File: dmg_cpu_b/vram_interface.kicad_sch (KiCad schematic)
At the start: 177 parts

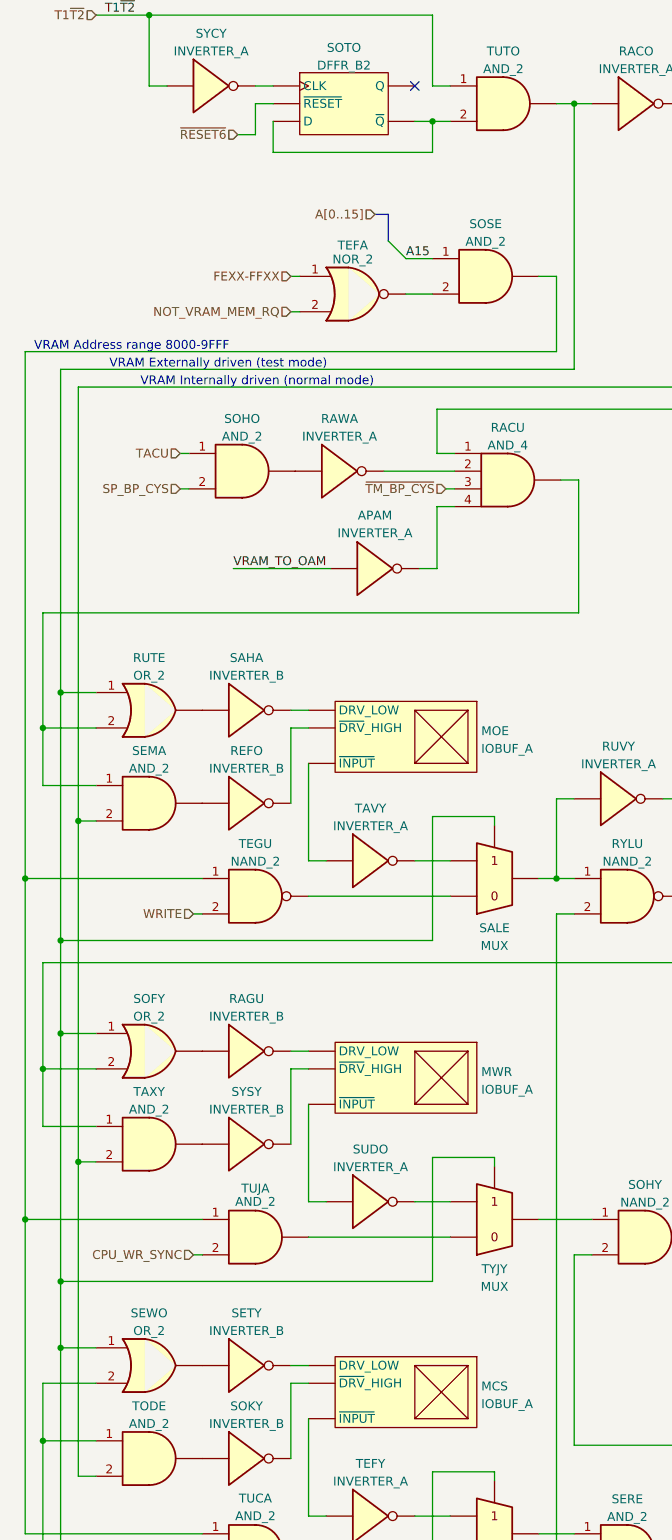
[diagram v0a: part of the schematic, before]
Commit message: Issues addressed. Renaming and inverted signal names to make thing more consistent and meaningful.
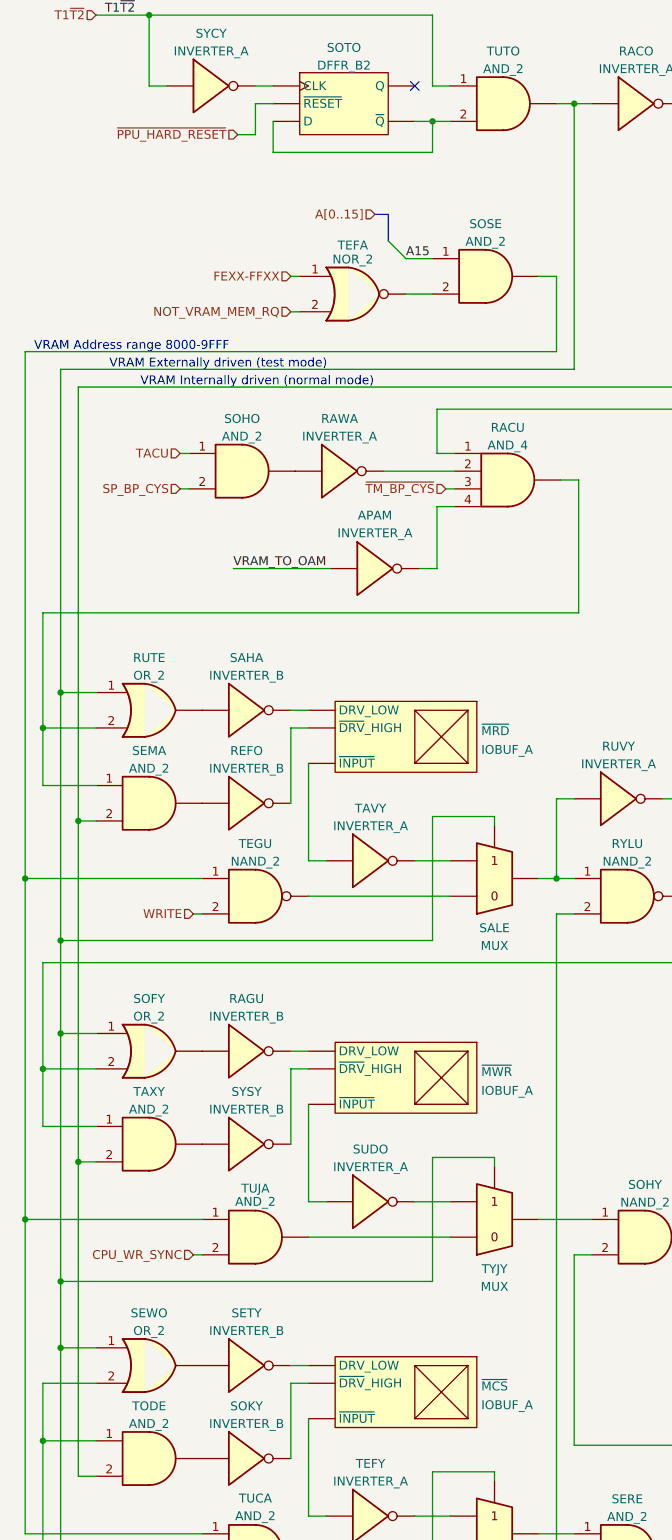
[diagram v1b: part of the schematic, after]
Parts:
- renumbered MCS to ~{MCS}, MOE to ~{MRD}, MWR to ~{MWR}
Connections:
- net ~{RESET6} renamed ~{PPU_HARD_RESET}
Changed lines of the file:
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@@
     (effects (font (size 1.27 1.27)) (justify right))
   )
-  (hierarchical_label "~{RESET6}" (shape input) (at 47.625 55.245 180)
+  (hierarchical_label "~{PPU_HARD_RESET}" (shape input) (at 47.625 55.245 180)
     (effects (font (size 1.27 1.27)) (justify right))
   )
@@
   (symbol (lib_id "DMG_CPU_Cells:IOBUF_A") (at 71.755 141.605 0) (mirror y) (unit 1)
     (in_bom yes) (on_board yes) (fields_autoplaced)
-    (property "Reference" "MOE" (id 0) (at 82.55 140.7703 0)
-      (effects (font (size 1.27 1.27)) (justify right))
-    )
-    (property "Value" "IOBUF_A" (id 1) (at 82.55 143.3072 0)
+    (property "Reference" "~{MRD}" (id 0) (at 82.55 140.7703 0)
+      (effects (font (size 1.27 1.27)) (justify right))
+    )
+    (property "Value" "IOBUF_A" (id 1) (at 82.55 143.4612 0)
       (effects (font (size 1.27 1.27)) (justify right))
     )
@@
   (symbol (lib_id "DMG_CPU_Cells:IOBUF_A") (at 71.755 235.585 0) (mirror y) (unit 1)
     (in_bom yes) (on_board yes) (fields_autoplaced)
-    (property "Reference" "MCS" (id 0) (at 82.55 234.7503 0)
-      (effects (font (size 1.27 1.27)) (justify right))
-    )
-    (property "Value" "IOBUF_A" (id 1) (at 82.55 237.2872 0)
+    (property "Reference" "~{MCS}" (id 0) (at 82.55 234.7503 0)
+      (effects (font (size 1.27 1.27)) (justify right))
+    )
+    (property "Value" "IOBUF_A" (id 1) (at 82.55 237.4412 0)
       (effects (font (size 1.27 1.27)) (justify right))
     )
@@
   (symbol (lib_id "DMG_CPU_Cells:IOBUF_A") (at 71.755 190.5 0) (mirror y) (unit 1)
     (in_bom yes) (on_board yes) (fields_autoplaced)
-    (property "Reference" "MWR" (id 0) (at 82.55 189.6653 0)
-      (effects (font (size 1.27 1.27)) (justify right))
-    )
-    (property "Value" "IOBUF_A" (id 1) (at 82.55 192.2022 0)
-      (effects (font (size 1.27 1.27)) (justify right))
-    )
+    (property "Reference" "~{MWR}" (id 0) (at 82.55 189.6653 0)
+      (effects (font (size 1.27 1.27)) (justify right))
+    )
+    (property "Value" "IOBUF_A" (id 1) (at 82.55 192.3562 0)
+      (effects (font (size 1.27 1.27)) (justify right))
+    )

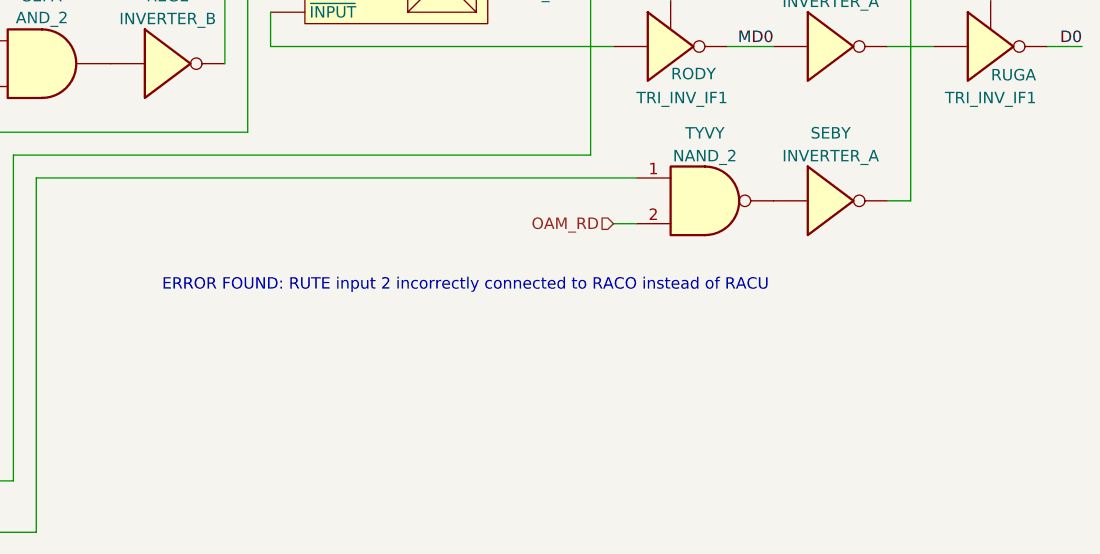
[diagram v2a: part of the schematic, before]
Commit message: Unnecessary comments removed. Data buffers moved to CPU page.
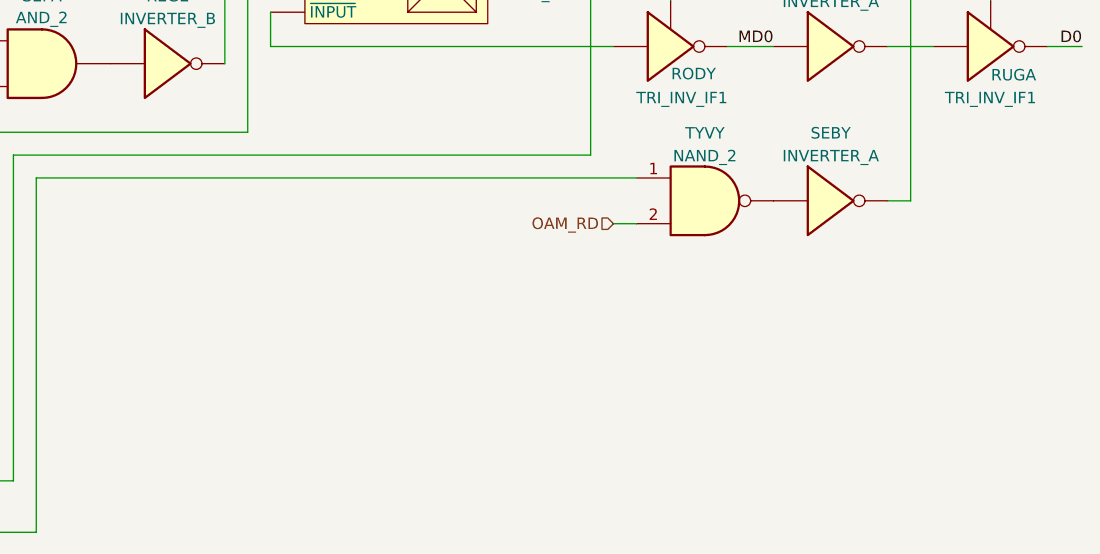
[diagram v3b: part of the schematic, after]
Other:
- note removed: "ERROR FOUND: RUTE input 2 incorrectly connected to RACO instead of RACU"
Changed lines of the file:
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@@
-    (effects (font (size 1.27 1.27)) (justify left bottom))
-  )
-  (text "ERROR FOUND: RUTE input 2 incorrectly connected to RACO instead of RACU"
-    (at 303.53 256.54 0)
     (effects (font (size 1.27 1.27)) (justify left bottom))
   )

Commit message: Update - edits were done some time ago so cannot rcall what has been done.
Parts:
- renumbered SAHA to RONU, SETY to ROSU
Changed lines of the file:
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@@
   (symbol (lib_id "DMG_CPU_Cells:INVERTER_B") (at 48.895 137.795 0) (unit 1)
     (in_bom yes) (on_board yes) (fields_autoplaced)
-    (property "Reference" "SAHA" (id 0) (at 48.895 130.2852 0))
+    (property "Reference" "RONU" (id 0) (at 48.895 130.2852 0))
     (property "Value" "INVERTER_B" (id 1) (at 48.895 132.8221 0))
     (property "Footprint" "" (id 2) (at 46.355 137.795 0)
@@
   (symbol (lib_id "DMG_CPU_Cells:INVERTER_B") (at 48.895 231.775 0) (unit 1)
     (in_bom yes) (on_board yes) (fields_autoplaced)
-    (property "Reference" "SETY" (id 0) (at 48.895 224.2652 0))
+    (property "Reference" "ROSU" (id 0) (at 48.895 224.2652 0))
     (property "Value" "INVERTER_B" (id 1) (at 48.895 226.8021 0))
     (property "Footprint" "" (id 2) (at 46.355 231.775 0)

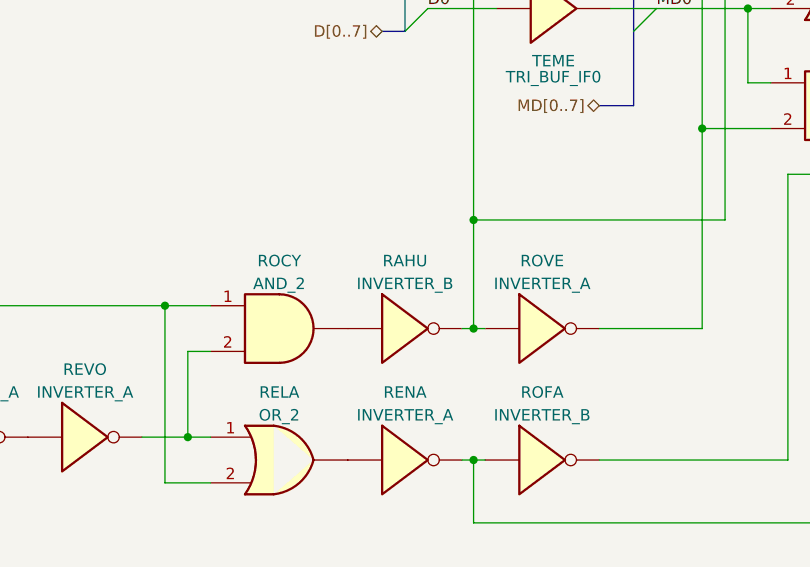
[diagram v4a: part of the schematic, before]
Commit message: Fix done based on github tickets #152 to #155
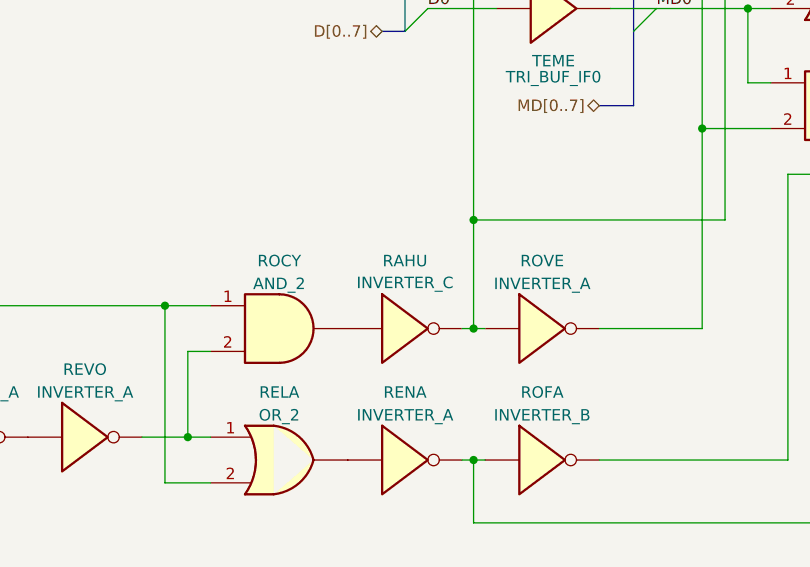
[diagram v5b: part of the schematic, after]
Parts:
- RAHU: value INVERTER_B -> INVERTER_C; symbol DMG_CPU_Cells:INVERTER_B -> DMG_CPU_Cells:INVERTER_C
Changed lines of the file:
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@@
     (pin "4")
   )
-  (symbol (lib_id "DMG_CPU_Cells:INVERTER_B") (at 241.935 255.905 0) (unit 1)
-    (in_bom yes) (on_board yes) (fields_autoplaced)
+  (symbol (lib_id "DMG_CPU_Cells:INVERTER_C") (at 241.935 255.905 0) (unit 1)
+    (in_bom yes) (on_board yes)
     (property "Reference" "RAHU" (id 0) (at 241.935 248.3952 0))
-    (property "Value" "INVERTER_B" (id 1) (at 241.935 250.9321 0))
+    (property "Value" "INVERTER_C" (id 1) (at 241.935 250.825 0))
     (property "Footprint" "" (id 2) (at 239.395 255.905 0)
       (effects (font (size 1.27 1.27)) hide)
     )
-    (property "Datasheet" "http://iceboy.a-singer.de/doc/dmg_cells.html#inv_b" (id 3) (at 243.205 263.525 0)
+    (property "Datasheet" "http://iceboy.a-singer.de/doc/dmg_cells.html#inv_c" (id 3) (at 243.205 263.525 0)
       (effects (font (size 1.27 1.27)) hide)
     )

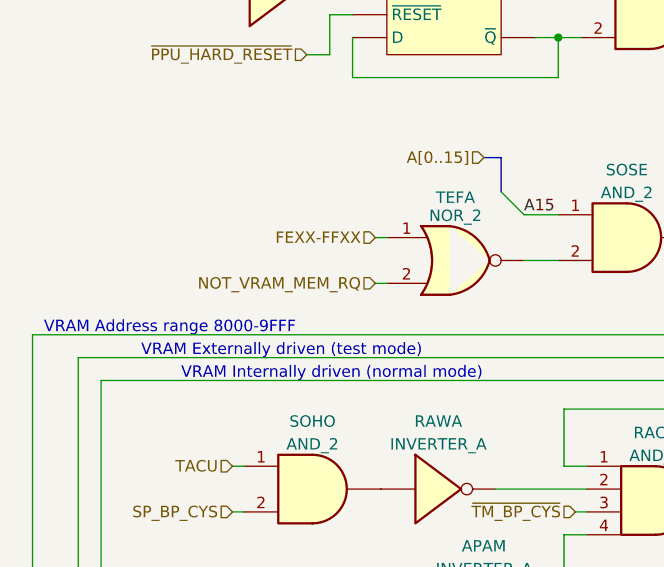
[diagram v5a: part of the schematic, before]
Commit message: fixes issues #155 #158 and #159
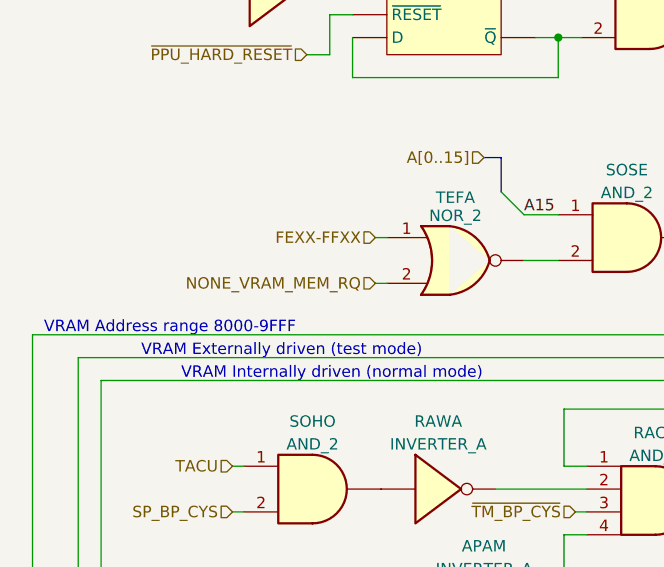
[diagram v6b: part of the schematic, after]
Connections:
- net NOT_VRAM_MEM_RQ renamed NONE_VRAM_MEM_RQ
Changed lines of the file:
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@@
     (effects (font (size 1.27 1.27)) (justify right))
   )
-  (hierarchical_label "NOT_VRAM_MEM_RQ" (shape input) (at 55.245 80.645 180)
+  (hierarchical_label "NONE_VRAM_MEM_RQ" (shape input) (at 55.245 80.645 180)
     (effects (font (size 1.27 1.27)) (justify right))
   )

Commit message: Changed NONE to NON in net name.
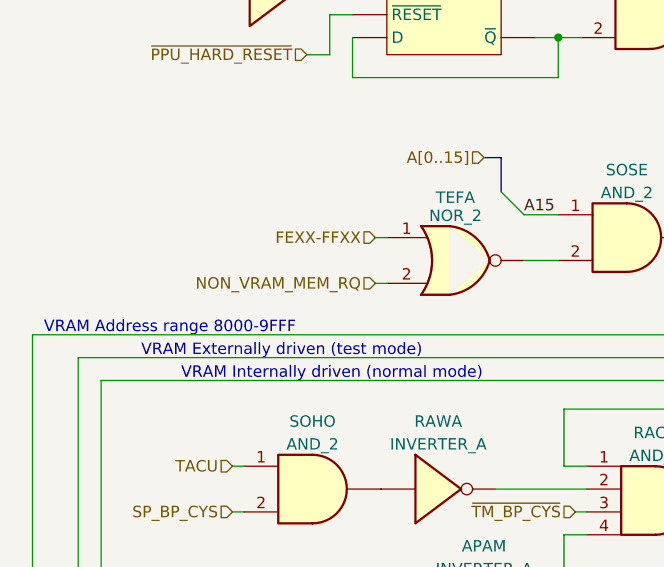
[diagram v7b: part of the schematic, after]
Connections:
- net NONE_VRAM_MEM_RQ renamed NON_VRAM_MEM_RQ
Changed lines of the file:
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@@
     (effects (font (size 1.27 1.27)) (justify right))
   )
-  (hierarchical_label "NONE_VRAM_MEM_RQ" (shape input) (at 55.245 80.645 180)
+  (hierarchical_label "NON_VRAM_MEM_RQ" (shape input) (at 55.245 80.645 180)
     (effects (font (size 1.27 1.27)) (justify right))
   )
